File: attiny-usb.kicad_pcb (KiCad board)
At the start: 2 copper layers, 40 x 12.2 mm, 12 parts, among them J1 Conn_01x05, U1 ATtiny85-20P

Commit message: design new pcb
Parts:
- moved C1 18.0 mm to (122.0, 99.4), turned to 180 degrees
- moved C2 13.6 mm to (133.2, 112.4), turned to 0 degrees
- moved D1 12.5 mm to (126.6, 112.6)
- moved R4 10.5 mm to (116.4, 112.8)
- moved R1 10.3 mm to (116.4, 99.4), turned to 180 degrees
- moved D2 8.70 mm to (117.4, 101.8)
- moved R2 6.54 mm to (118.0, 110.6), turned to 0 degrees
- moved R3 5.95 mm to (129.0, 99.4)
- moved D3 2.70 mm to (133.2, 106.2)
- moved U1 2.51 mm to (121.2, 102.2)
- moved J1 1.95 mm to (138.0, 101.1)
- moved U2 0.32 mm to (104.0, 106.2)
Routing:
- net GND: track 22.0 -> 8.63 mm
- net Net-(D1-K): track 15.8 -> 26.2 mm
- net +5V: track 64.4 -> 68.9 mm, vias 0 -> 1
- net Net-(D3-DIN): track 2.76 -> 5.06 mm
- net Net-(U1-PB1): track 7.06 -> 9.15 mm
- net Net-(D2-K): track 14.7 -> 15.7 mm
- net Net-(U1-XTAL2/PB4): track 10.3 -> 9.45 mm
- net Net-(J1-Pin_3): track 9.07 -> 9.63 mm
- net Net-(J1-Pin_4): track 18.9 -> 19.4 mm
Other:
- board size 40 x 12.2 mm -> 38 x 16.2 mm

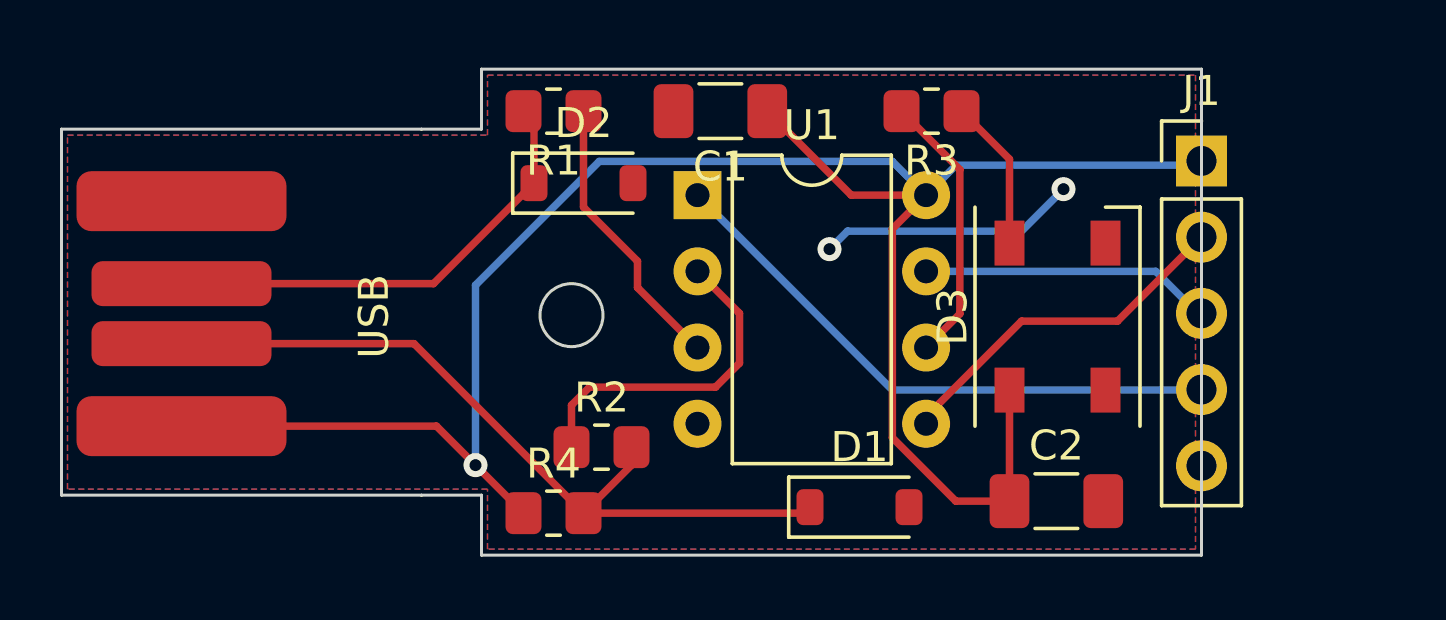
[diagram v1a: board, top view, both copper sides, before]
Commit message: create 2x3 panel
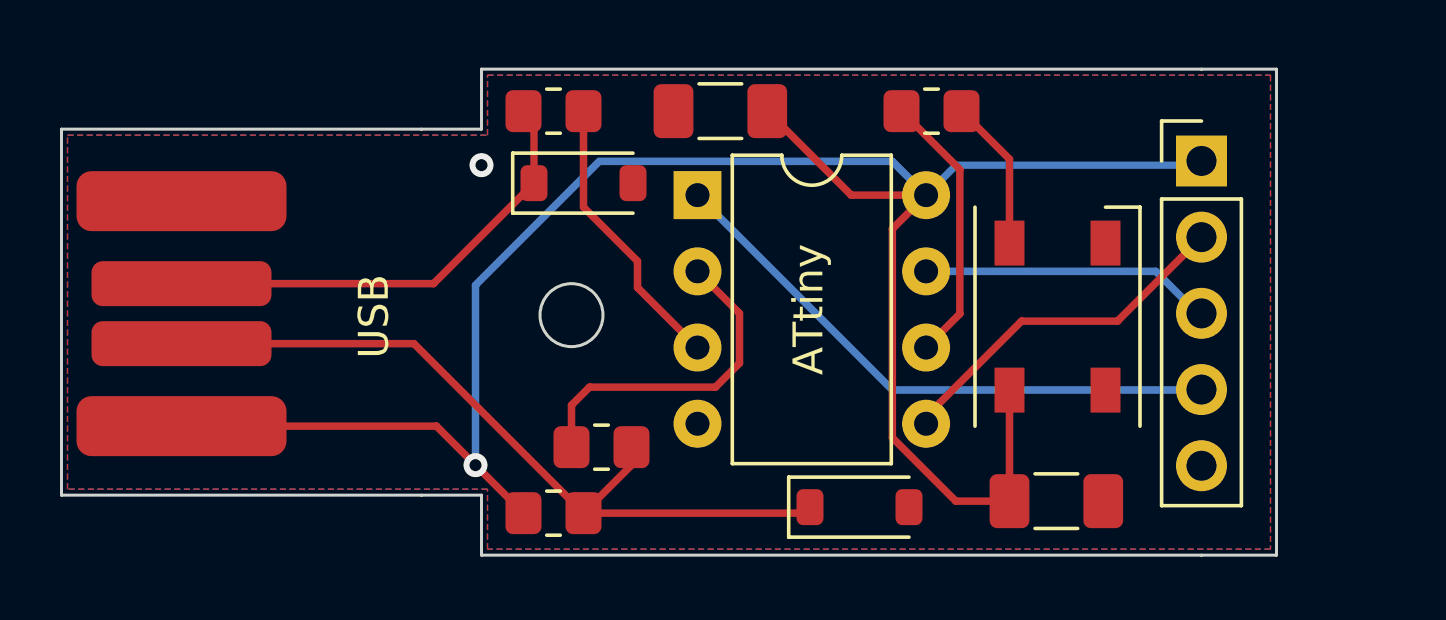
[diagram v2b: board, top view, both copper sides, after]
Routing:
- net GND: track 8.63 -> 0.00 mm, vias 2 -> 1
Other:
- board size 38 x 16.2 mm -> 40.5 x 16.2 mm
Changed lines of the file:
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@@
     (property "ki_keywords" "R res resistor")
     (attr smd)
-    (fp_text reference "R2" (at 0 -1.65) (layer "F.SilkS")
-        (effects (font (size 1 1) (thickness 0.15)))
-    )
-    (fp_text value "68R" (at 0 1.65) (layer "F.Fab")
+    (fp_text reference "R2" (at 0 -1.65) (layer "F.SilkS") hide
+        (effects (font (size 1 1) (thickness 0.15)))
+    )
+    (fp_text value "68R" (at 0 1.65) (layer "F.Fab") hide
         (effects (font (size 1 1) (thickness 0.15)))
     )
@@
     (property "ki_keywords" "diode")
     (attr smd)
-    (fp_text reference "D1" (at 0 -2) (layer "F.SilkS")
-        (effects (font (size 1 1) (thickness 0.15)))
-    )
-    (fp_text value "3V6" (at 0 2.1) (layer "F.Fab")
-        (effects (font (size 1 1) (thickness 0.15)))
-    )
-    (fp_text user "${REFERENCE}" (at 0 -2) (layer "F.Fab")
+    (fp_text reference "D1" (at 0 -2) (layer "F.SilkS") hide
+        (effects (font (size 1 1) (thickness 0.15)))
+    )
+    (fp_text value "3V6" (at 0 2.1) (layer "F.Fab") hide
         (effects (font (size 1 1) (thickness 0.15)))
     )
@@
     (property "ki_keywords" "connector")
     (attr through_hole)
-    (fp_text reference "J1" (at 0 -2.33) (layer "F.SilkS")
-        (effects (font (size 1 1) (thickness 0.15)))
-    )
-    (fp_text value "Conn_01x05" (at 0 12.49) (layer "F.Fab")
+    (fp_text reference "J1" (at 0 -2.33) (layer "F.SilkS") hide
+        (effects (font (size 1 1) (thickness 0.15)))
+    )
+    (fp_text value "Conn_01x05" (at 0 12.49) (layer "F.Fab") hide
         (effects (font (size 1 1) (thickness 0.15)))
     )
@@
     (property "ki_keywords" "R res resistor")
     (attr smd)
-    (fp_text reference "R1" (at 0 -1.65) (layer "F.SilkS")
-        (effects (font (size 1 1) (thickness 0.15)))
-    )
-    (fp_text value "68R" (at 0 1.65) (layer "F.Fab")
+    (fp_text reference "R1" (at 0 -1.65) (layer "F.SilkS") hide
+        (effects (font (size 1 1) (thickness 0.15)))
+    )
+    (fp_text value "68R" (at 0 1.65) (layer "F.Fab") hide
         (effects (font (size 1 1) (thickness 0.15)))
     )
@@
     (property "ki_keywords" "R res resistor")
     (attr smd)
-    (fp_text reference "R4" (at 0 -1.65) (layer "F.SilkS")
-        (effects (font (size 1 1) (thickness 0.15)))
-    )
-    (fp_text value "1k5" (at 0 1.65) (layer "F.Fab")
+    (fp_text reference "R4" (at 0 -1.65) (layer "F.SilkS") hide
+        (effects (font (size 1 1) (thickness 0.15)))
+    )
+    (fp_text value "1k5" (at 0 1.65) (layer "F.Fab") hide
         (effects (font (size 1 1) (thickness 0.15)))
     )
@@
     (property "ki_keywords" "AVR 8bit Microcontroller tinyAVR")
     (attr through_hole)
-    (fp_text reference "U1" (at 3.81 -2.33) (layer "F.SilkS")
-        (effects (font (size 1 1) (thickness 0.15)))
-    )
-    (fp_text value "ATtiny85-20P" (at 3.81 9.95) (layer "F.Fab")
-        (effects (font (size 1 1) (thickness 0.15)))
-    )
-    (fp_text user "${REFERENCE}" (at 3.81 3.81) (layer "F.Fab")
+    (fp_text reference "U1" (at 3.81 -2.33) (layer "F.SilkS") hide
+        (effects (font (size 1 1) (thickness 0.15)))
+    )
+    (fp_text value "ATtiny85-20P" (at 3.81 9.95) (layer "F.Fab") hide
+        (effects (font (size 1 1) (thickness 0.15)))
+    )
+    (fp_text user "ATtiny" (at 3.7 3.81 90) (layer "F.SilkS")
         (effects (font (size 1 1) (thickness 0.15)))
     )
@@
     (property "ki_keywords" "diode")
     (attr smd)
-    (fp_text reference "D2" (at 0 -2) (layer "F.SilkS")
-        (effects (font (size 1 1) (thickness 0.15)))
-    )
-    (fp_text value "3V6" (at 0 2.1) (layer "F.Fab")
-        (effects (font (size 1 1) (thickness 0.15)))
-    )
-    (fp_text user "${REFERENCE}" (at 0 -2) (layer "F.Fab")
+    (fp_text reference "D2" (at 0 -2) (layer "F.SilkS") hide
+        (effects (font (size 1 1) (thickness 0.15)))
+    )
+    (fp_text value "3V6" (at 0 2.1) (layer "F.Fab") hide
         (effects (font (size 1 1) (thickness 0.15)))
     )
@@
     (property "ki_keywords" "R res resistor")
     (attr smd)
-    (fp_text reference "R3" (at 0 -1.65) (layer "F.SilkS")
-        (effects (font (size 1 1) (thickness 0.15)))
-    )
-    (fp_text value "400R" (at 0 1.65) (layer "F.Fab")
+    (fp_text reference "R3" (at 0 -1.65) (layer "F.SilkS") hide
+        (effects (font (size 1 1) (thickness 0.15)))
+    )
+    (fp_text value "400R" (at 0 1.65) (layer "F.Fab") hide
         (effects (font (size 1 1) (thickness 0.15)))
     )
@@
     (property "ki_keywords" "cap capacitor")
     (attr smd)
-    (fp_text reference "C2" (at 0 -1.85) (layer "F.SilkS")
-        (effects (font (size 1 1) (thickness 0.15)))
-    )
-    (fp_text value "100n" (at 0 1.85) (layer "F.Fab")
+    (fp_text reference "C2" (at 0 -1.85) (layer "F.SilkS") hide
+        (effects (font (size 1 1) (thickness 0.15)))
+    )
+    (fp_text value "100n" (at 0 1.85) (layer "F.Fab") hide
         (effects (font (size 1 1) (thickness 0.15)))
     )
@@
     (property "ki_keywords" "cap capacitor")
     (attr smd)
-    (fp_text reference "C1" (at 0 -1.85) (layer "F.SilkS")
-        (effects (font (size 1 1) (thickness 0.15)))
-    )
-    (fp_text value "100n" (at 0 1.85) (layer "F.Fab")
+    (fp_text reference "C1" (at 0 -1.85) (layer "F.SilkS") hide
+        (effects (font (size 1 1) (thickness 0.15)))
+    )
+    (fp_text value "100n" (at 0 1.85) (layer "F.Fab") hide
         (effects (font (size 1 1) (thickness 0.15)))
     )
@@
     (property "ki_keywords" "RGB LED NeoPixel addressable")
     (attr smd)
-    (fp_text reference "D3" (at 0 -3.5 90) (layer "F.SilkS")
+    (fp_text reference "D3" (at 0 -3.5 90) (layer "F.SilkS") hide
         (effects (font (size 1 1) (thickness 0.15)))
     )
@@
   (gr_line (start 112 112.2) (end 114 112.2)
     (stroke (width 0.1) (type default)) (layer "Edge.Cuts"))
+  (gr_line (start 138 98) (end 140.5 98)
+    (stroke (width 0.1) (type default)) (layer "Edge.Cuts"))
   (gr_circle (center 117 106.2) (end 118.05 106.2)
     (stroke (width 0.1) (type default)) (fill none) (layer "Edge.Cuts"))
+  (gr_line (start 140.5 98) (end 140.5 114.2)
+    (stroke (width 0.1) (type default)) (layer "Edge.Cuts"))
   (gr_line (start 114 100) (end 114 98)
     (stroke (width 0.1) (type default)) (layer "Edge.Cuts"))
@@
   (gr_line (start 114 98) (end 138 98)
     (stroke (width 0.1) (type default)) (layer "Edge.Cuts"))
-  (gr_line (start 138 114.2) (end 138 98)
-    (stroke (width 0.1) (type default)) (layer "Edge.Cuts"))
   (gr_line (start 100 100) (end 100 112.2)
+    (stroke (width 0.1) (type default)) (layer "Edge.Cuts"))
+  (gr_line (start 140.5 114.2) (end 138 114.2)
     (stroke (width 0.1) (type default)) (layer "Edge.Cuts"))
   (segment (start 113.8 111.2) (end 115.4 112.8) (width 0.25) (layer "F.Cu") (net 1))
@@
   (segment (start 128.82 102.2) (end 129.8 101.22) (width 0.25) (layer "B.Cu") (net 1))
   (segment (start 117.925 101.075) (end 127.695 101.075) (width 0.25) (layer "B.Cu") (net 1))
-  (via (at 133.4 102) (size 0.8) (drill 0.4) (layers "F.Cu" "B.Cu") (free) (net 2))
-  (via (at 125.6 104) (size 0.8) (drill 0.4) (layers "F.Cu" "B.Cu") (free) (net 2))
-  (segment (start 132 103.4) (end 133.4 102) (width 0.25) (layer "B.Cu") (net 2))
-  (segment (start 126.2 103.4) (end 132 103.4) (width 0.25) (layer "B.Cu") (net 2))
-  (segment (start 125.6 104) (end 126.2 103.4) (width 0.25) (layer "B.Cu") (net 2))
+  (via (at 114 101.2) (size 0.8) (drill 0.4) (layers "F.Cu" "B.Cu") (free) (net 2))
   (segment (start 111.75 107.15) (end 104 107.15) (width 0.25) (layer "F.Cu") (net 3))
   (segment (start 124.75 112.8) (end 124.95 112.6) (width 0.25) (layer "F.Cu") (net 3))
@@
         (xy 114.2 100.2)
         (xy 114.2 98.2)
-        (xy 137.8 98.2)
-        (xy 137.8 114)
+        (xy 140.3 98.2)
+        (xy 140.3 114)
         (xy 114.2 114)
         (xy 114.2 112)

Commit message: create pcb outline for version 2.0.0
Thinking about moving large pin header one step towards the usb
connector.
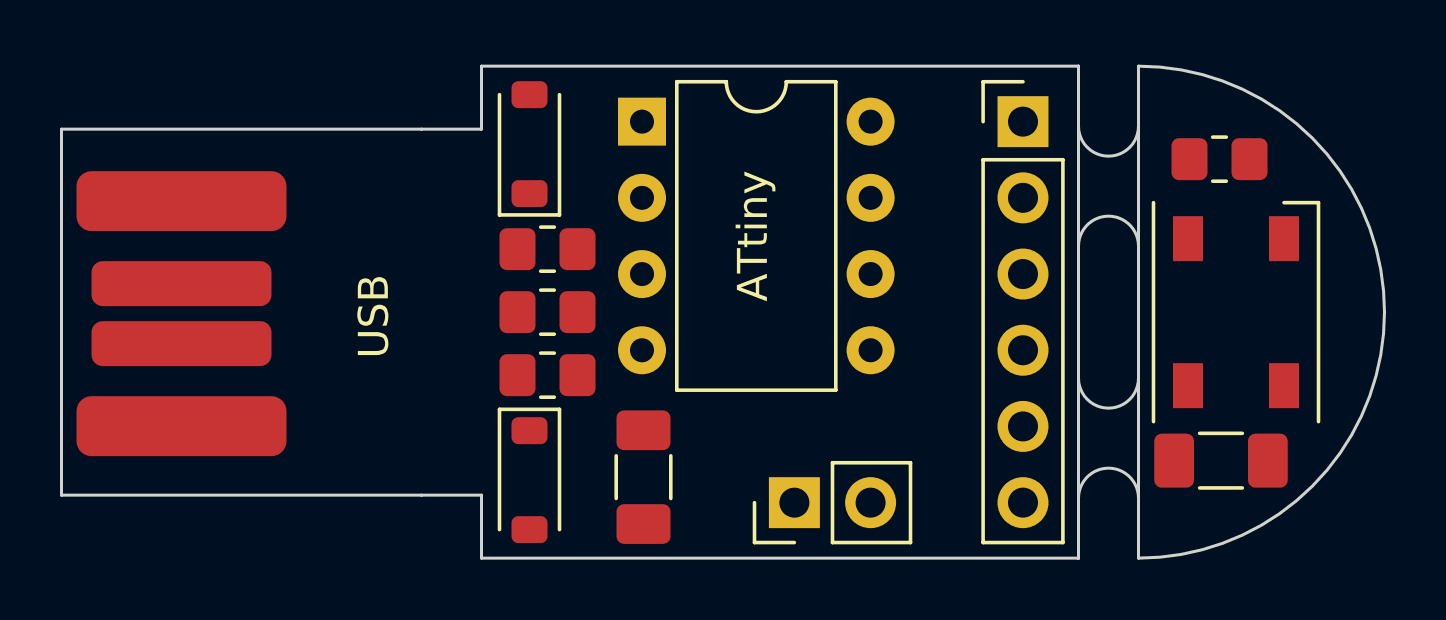
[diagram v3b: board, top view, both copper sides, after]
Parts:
- removed J1: Conn_01x05, Connector_PinHeader_2.54mm:PinHeader_1x05_P2.54mm_Vertical
- added J2: Conn_01x06, Connector_PinHeader_2.54mm:PinHeader_1x06_P2.54mm_Vertical, F.Cu at (132.1, 99.8)
- added J3: Conn_01x02, Connector_PinHeader_2.54mm:PinHeader_1x02_P2.54mm_Vertical, F.Cu at (124.4, 112.5)
- D3: value SK6812 -> WS2812B
- moved C1 12.5 mm to (119.4, 111.6), turned to -90 degrees
- moved D1 11.0 mm to (115.6, 111.7), turned to -90 degrees
- moved R3 9.73 mm to (138.6, 101.0), turned to 0 degrees
- moved D3 5.95 mm to (139.2, 106.1)
- moved C2 5.65 mm to (138.7, 111.0)
- moved R2 4.85 mm to (116.2, 106.1), turned to 180 degrees
- moved R1 4.60 mm to (116.2, 104.0)
- moved R4 4.60 mm to (116.2, 108.2)
- moved U1 3.07 mm to (119.3, 99.8)
- moved D2 2.22 mm to (115.6, 100.5), turned to 90 degrees
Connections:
- R3 pad 1: Net-(D3-DIN) -> Net-(J2-Pin_2)
- R3 pad 2: Net-(U1-PB1) -> Net-(D3-DIN)
- U1 pad 6: Net-(U1-PB1) -> Net-(J2-Pin_2)
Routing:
- net +5V: track 68.9 -> 0.00 mm, vias 1 -> 0
- net Net-(D1-K): track 26.2 -> 0.00 mm
- net Net-(J2-Pin_6): track 19.4 -> 0.00 mm
- net Net-(D2-K): track 15.7 -> 0.00 mm
- net Net-(J2-Pin_1): track 11.8 -> 0.00 mm
- net Net-(J2-Pin_4): track 11.2 -> 0.00 mm
- net Net-(J2-Pin_3): track 9.63 -> 0.00 mm
- net Net-(J2-Pin_5): track 9.45 -> 0.00 mm
- net Net-(U1-PB1): track 9.15 -> 0.00 mm
- net Net-(D3-DIN): track 5.06 -> 0.00 mm
- net GND: vias 1 -> 0
- removed copper zone on B.Cu, net GND
- removed copper zone on F.Cu, net GND
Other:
- board size 40.5 x 16.2 mm -> 44.1 x 16.4 mm

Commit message: move large pin header and remove resistor for Neopixel
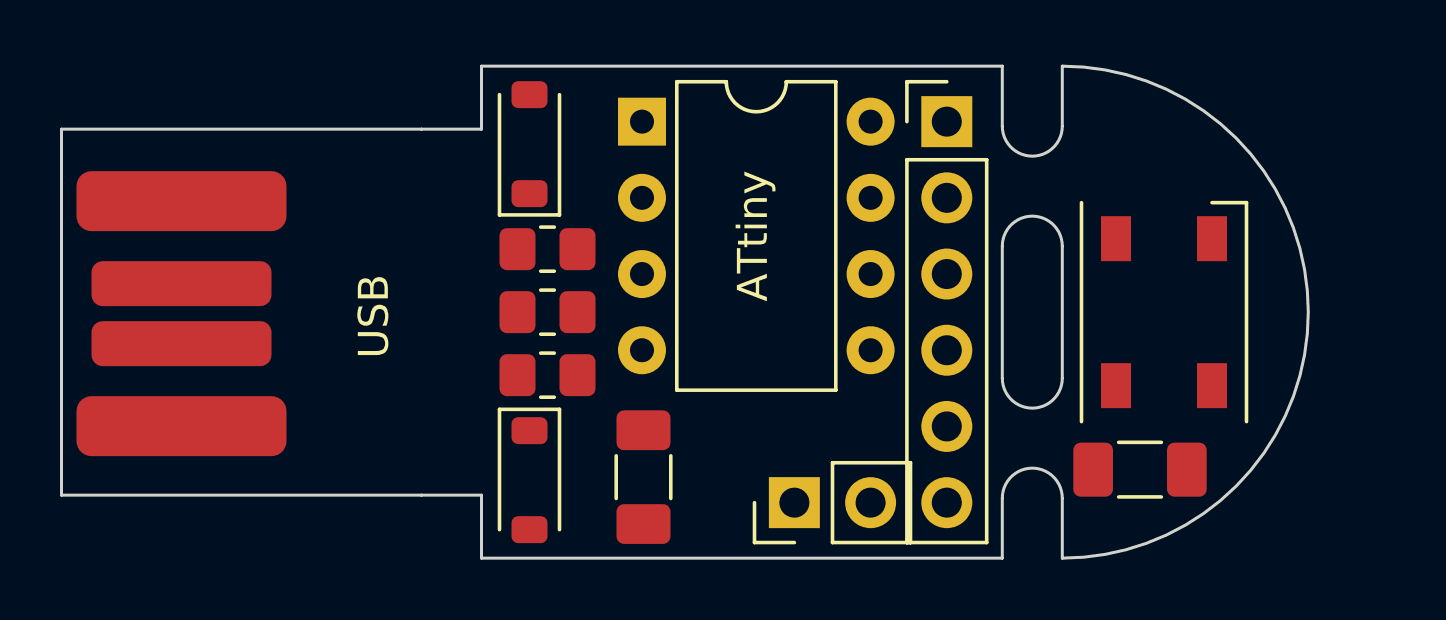
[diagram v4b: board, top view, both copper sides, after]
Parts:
- removed R3: 400R, Resistor_SMD:R_0805_2012Metric_Pad1.20x1.40mm_HandSolder
- D3: value WS2812B -> SK6812
- moved C2 2.72 mm to (135.9, 111.3)
- moved J2 2.54 mm to (129.5, 99.8)
- moved D3 2.40 mm to (136.8, 106.1)
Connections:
- J2 pad 2: Net-(J2-Pin_2) -> Net-(D3-DIN)
- U1 pad 6: Net-(J2-Pin_2) -> Net-(D3-DIN)
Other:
- board size 44.1 x 16.4 mm -> 41.6 x 16.4 mm
